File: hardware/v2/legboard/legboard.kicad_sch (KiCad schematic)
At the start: 17 parts, among them J1 UPLINK_RJ11, J2 COXA, J3 FEMUR, J4 TIBIA, J5 SERVO_PWR_IN, U1 XIAO-RP2040, U2 SP3485CN, U3 INA4181A3IPWR

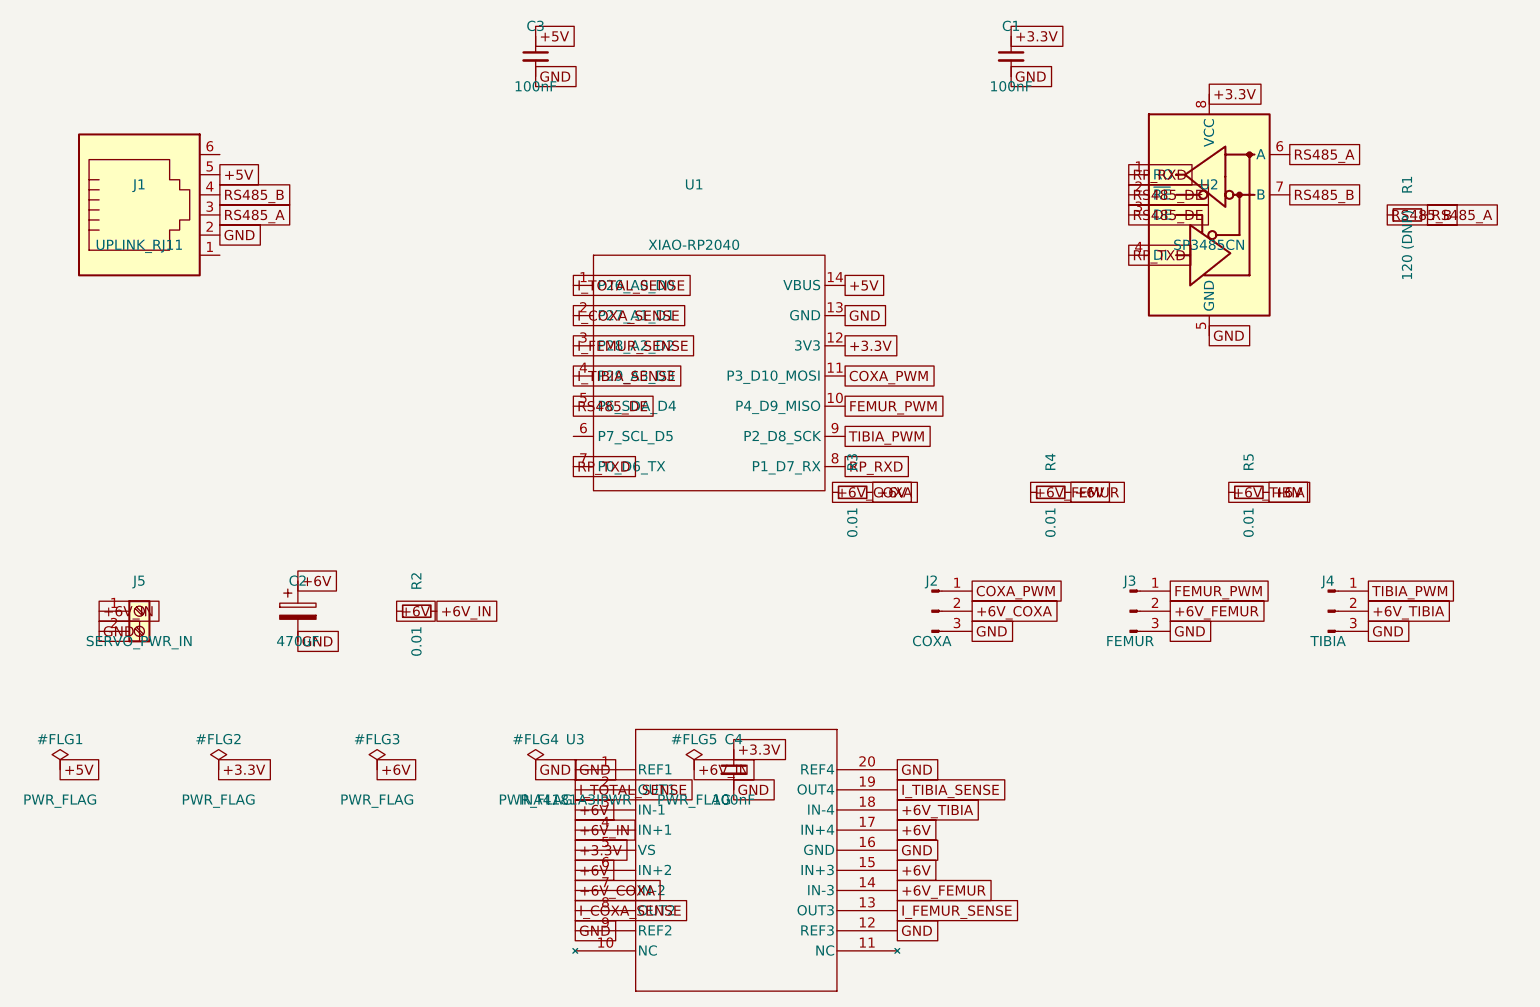
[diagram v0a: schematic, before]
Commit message: LegBoard: Kelvin shunts for current sensing to fix sense-net routing
Convert the four current-sense shunts (R2 total + R3/R4/R5 per-servo
branches) from 2-terminal 0805/1210 resistors to 4-terminal Kelvin
shunts (Device:R_Shunt, footprint Resistor_SMD:R_Shunt_Ohmite_LVK12).

Why: the three branch shunts share one physical +6V source node, so all
three INA4181 IN+ pins (U3 6/15/17) sat on the shared +6V net. The
autorouter was free to bridge those high-side sense taps together and
assign them current-rail trace widths. A 2-terminal shunt cannot fix
this because force current and sense share the same pad/net.

With Kelvin shunts the force pads (pins 1/4) carry the +6V rails while
each sense pad (pins 2/3) drives a unique two-node net to its INA input:
ITOT_SP/SN, COXA_SP/SN, FEMUR_SP/SN, TIBIA_SP/SN. IN+ stays on the
higher-potential (source) side of every channel.

Shunts are placed at rotation 0: the DSL pin-rotation transform
mis-resolves off-axis pins at 90/270 (the sense pads land off-pin and
the force pads swap), which showed up as single-node/unconnected sense
nets in the netlist export. Documented in the board script and README.

Verified: netlist export confirms all 8 sense nets are clean and
correctly polarized; uuids.json grew by additions only (no UUID
rewrites, PCB layout links preserved); ERC violation count unchanged.

Co-Authored-By: Claude Opus 4.8 <noreply@anthropic.com>
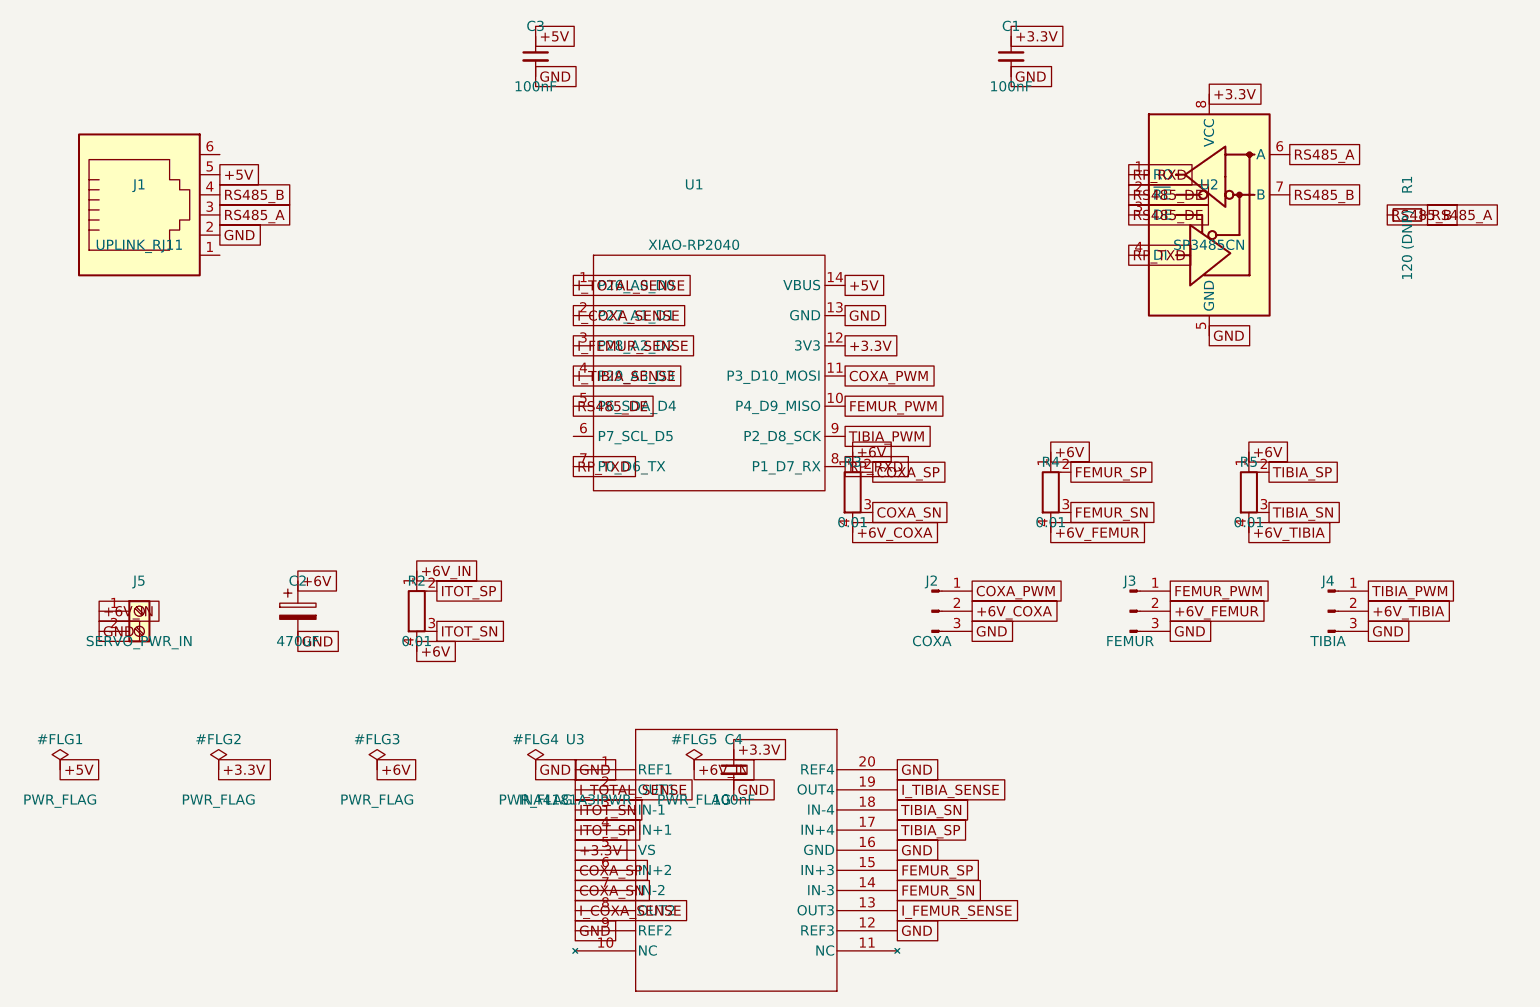
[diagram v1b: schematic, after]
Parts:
- R2, R3, R4, R5: footprint Resistor_SMD:R_1210_3225Metric_Pad1.30x2.65mm_HandSolder -> Resistor_SMD:R_Shunt_Ohmite_LVK12; symbol Device:R_Small -> Device:R_Shunt
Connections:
- net +6V: now also R2.4, R3.1, R4.1, R5.1; no longer R2.1, R3.2, R4.2, R5.2, U3.15 (IN+3), U3.17 (IN+4), U3.3 (IN-1), U3.6 (IN+2)
- net +6V_COXA: now also R3.4; no longer R3.1, U3.7 (IN-2)
- net +6V_FEMUR: now also R4.4; no longer R4.1, U3.14 (IN-3)
- net +6V_IN: now also R2.1; no longer R2.2, U3.4 (IN+1)
- net +6V_TIBIA: now also R5.4; no longer R5.1, U3.18 (IN-4)
- new net COXA_SN: R3.3, U3.7 (IN-2)
- new net COXA_SP: R3.2, U3.6 (IN+2)
- new net FEMUR_SN: R4.3, U3.14 (IN-3)
- new net FEMUR_SP: R4.2, U3.15 (IN+3)
- new net ITOT_SN: R2.3, U3.3 (IN-1)
- new net ITOT_SP: R2.2, U3.4 (IN+1)
- new net TIBIA_SN: R5.3, U3.18 (IN-4)
- new net TIBIA_SP: R5.2, U3.17 (IN+4)
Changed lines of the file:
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@@
 	)
 	(symbol
-		(lib_id "Device:R_Small")
-		(at 85 140 90)
+		(lib_id "Device:R_Shunt")
+		(at 85 140 0)
 		(unit 1)
 		(exclude_from_sim no)
@@
 			)
 		)
-		(property "Footprint" "Resistor_SMD:R_1210_3225Metric_Pad1.30x2.65mm_HandSolder"
+		(property "Footprint" "Resistor_SMD:R_Shunt_Ohmite_LVK12"
 			(at 85 140 0)
 			(effects
@@
 	(global_label "+6V_IN"
 		(shape passive)
-		(at 87.54 140 0)
+		(at 85 134.92 0)
 		(fields_autoplaced yes)
 		(effects
@@
 	(global_label "+6V"
 		(shape passive)
-		(at 82.46 140 0)
+		(at 85 145.08 0)
+		(fields_autoplaced yes)
+		(effects
+			(font
+				(size 1.27 1.27)
+			)
+			(justify left)
+		)
+	)
+	(global_label "ITOT_SP"
+		(shape passive)
+		(at 87.54 137.46 0)
+		(fields_autoplaced yes)
+		(effects
+			(font
+				(size 1.27 1.27)
+			)
+			(justify left)
+		)
+	)
+	(global_label "ITOT_SN"
+		(shape passive)
+		(at 87.54 142.54 0)
 		(fields_autoplaced yes)
 		(effects
@@
 	)
 	(symbol
-		(lib_id "Device:R_Small")
-		(at 140 125 90)
+		(lib_id "Device:R_Shunt")
+		(at 140 125 0)
 		(unit 1)
 		(exclude_from_sim no)
@@
 			)
 		)
-		(property "Footprint" "Resistor_SMD:R_1210_3225Metric_Pad1.30x2.65mm_HandSolder"
+		(property "Footprint" "Resistor_SMD:R_Shunt_Ohmite_LVK12"
 			(at 140 125 0)
 			(effects
@@
 	(global_label "+6V"
 		(shape passive)
-		(at 142.54 125 0)
+		(at 140 119.92 0)
 		(fields_autoplaced yes)
 		(effects
@@
 	(global_label "+6V_COXA"
 		(shape passive)
-		(at 137.46 125 0)
+		(at 140 130.08 0)
+		(fields_autoplaced yes)
+		(effects
+			(font
+				(size 1.27 1.27)
+			)
+			(justify left)
+		)
+	)
+	(global_label "COXA_SP"
+		(shape passive)
+		(at 142.54 122.46 0)
+		(fields_autoplaced yes)
+		(effects
+			(font
+				(size 1.27 1.27)
+			)
+			(justify left)
+		)
+	)
+	(global_label "COXA_SN"
+		(shape passive)
+		(at 142.54 127.54 0)
 		(fields_autoplaced yes)
 		(effects
@@
 	)
 	(symbol
-		(lib_id "Device:R_Small")
-		(at 165 125 90)
+		(lib_id "Device:R_Shunt")
+		(at 165 125 0)
 		(unit 1)
 		(exclude_from_sim no)
@@
 			)
 		)
-		(property "Footprint" "Resistor_SMD:R_1210_3225Metric_Pad1.30x2.65mm_HandSolder"
+		(property "Footprint" "Resistor_SMD:R_Shunt_Ohmite_LVK12"
 			(at 165 125 0)
 			(effects
@@
 	(global_label "+6V"
 		(shape passive)
-		(at 167.54 125 0)
+		(at 165 119.92 0)
 		(fields_autoplaced yes)
 		(effects
@@
 	(global_label "+6V_FEMUR"
 		(shape passive)
-		(at 162.46 125 0)
+		(at 165 130.08 0)
+		(fields_autoplaced yes)
+		(effects
+			(font
+				(size 1.27 1.27)
+			)
+			(justify left)
+		)
+	)
+	(global_label "FEMUR_SP"
+		(shape passive)
+		(at 167.54 122.46 0)
+		(fields_autoplaced yes)
+		(effects
+			(font
+				(size 1.27 1.27)
+			)
+			(justify left)
+		)
+	)
+	(global_label "FEMUR_SN"
+		(shape passive)
+		(at 167.54 127.54 0)
 		(fields_autoplaced yes)
 		(effects
@@
 	)
 	(symbol
-		(lib_id "Device:R_Small")
-		(at 190 125 90)
+		(lib_id "Device:R_Shunt")
+		(at 190 125 0)
 		(unit 1)
 		(exclude_from_sim no)
@@
 			)
 		)
-		(property "Footprint" "Resistor_SMD:R_1210_3225Metric_Pad1.30x2.65mm_HandSolder"
+		(property "Footprint" "Resistor_SMD:R_Shunt_Ohmite_LVK12"
 			(at 190 125 0)
 			(effects
@@
 	(global_label "+6V"
 		(shape passive)
-		(at 192.54 125 0)
+		(at 190 119.92 0)
 		(fields_autoplaced yes)
 		(effects
@@
 	(global_label "+6V_TIBIA"
 		(shape passive)
-		(at 187.46 125 0)
+		(at 190 130.08 0)
+		(fields_autoplaced yes)
+		(effects
+			(font
+				(size 1.27 1.27)
+			)
+			(justify left)
+		)
+	)
+	(global_label "TIBIA_SP"
+		(shape passive)
+		(at 192.54 122.46 0)
+		(fields_autoplaced yes)
+		(effects
+			(font
+				(size 1.27 1.27)
+			)
+			(justify left)
+		)
+	)
+	(global_label "TIBIA_SN"
+		(shape passive)
+		(at 192.54 127.54 0)
 		(fields_autoplaced yes)
 		(effects
@@
 		)
 	)
-	(global_label "+6V_IN"
+	(global_label "ITOT_SP"
 		(shape passive)
 		(at 105 167.62 0)
@@
 		)
 	)
-	(global_label "+6V"
+	(global_label "ITOT_SN"
 		(shape passive)
 		(at 105 165.08 0)
@@
 		)
 	)
-	(global_label "+6V"
+	(global_label "COXA_SP"
 		(shape passive)
 		(at 105 172.7 0)
@@
 		)
 	)
-	(global_label "+6V_COXA"
+	(global_label "COXA_SN"
 		(shape passive)
 		(at 105 175.24 0)
@@
 		)
 	)
-	(global_label "+6V"
+	(global_label "FEMUR_SP"
 		(shape passive)
 		(at 145.64 172.7 0)
@@
 		)
 	)
-	(global_label "+6V_FEMUR"
+	(global_label "FEMUR_SN"
 		(shape passive)
 		(at 145.64 175.24 0)
@@
 		)
 	)
-	(global_label "+6V"
+	(global_label "TIBIA_SP"
 		(shape passive)
 		(at 145.64 167.62 0)
@@
 		)
 	)
-	(global_label "+6V_TIBIA"
+	(global_label "TIBIA_SN"
 		(shape passive)
 		(at 145.64 165.08 0)
